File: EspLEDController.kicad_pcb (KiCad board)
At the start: 4 copper layers, 100 x 95 mm, 106 parts, among them J1 USB_B_Micro, J10 Conn_01x02, J11 Conn_01x02, J12 Conn_01x02, J13 Conn_01x02, J14 Conn_01x02, J15 Conn_01x02, J16 Conn_01x02, J17 Conn_01x02, J18 Conn_01x02, J19 Conn_01x02, J2 FTDI, J20 Conn_01x02, J21 Conn_01x02, J22 Conn_01x02, J23 Conn_01x02, J24 Conn_01x02, J25 Conn_01x02, J26 Conn_01x02, J27 Conn_01x02, J28 Conn_01x02, J29 Conn_01x02, J3 FLASH, J30 Conn_01x02, J31 Conn_01x02, J32 Conn_01x02, J33 Conn_01x02, J34 Conn_01x02, J35 Conn_01x02, J36 Conn_01x02, J37 Conn_01x02, J38 Conn_01x02, J39 Conn_01x02, J4 Conn_01x02, J40 Conn_01x02, J41 Conn_01x02, J42 Conn_01x02, J43 Conn_01x02, J44 Conn_01x02, J45 Conn_01x02, J5 Conn_01x02, J6 Conn_01x02, J7 Conn_01x02, J8 Conn_01x02, J9 Conn_01x02, SW1 RESET, SW2 FLASH, U1 ESP-12F, U10 WS2811, U11 WS2811, U12 WS2811, U13 WS2811, U14 WS2811, U15 WS2811, U16 WS2811, U17 74AHCT1G125, U2 AMS1117-3.3, U3 WS2811, U4 WS2811, U5 WS2811, U6 WS2811, U7 WS2811, U8 WS2811, U9 WS2811

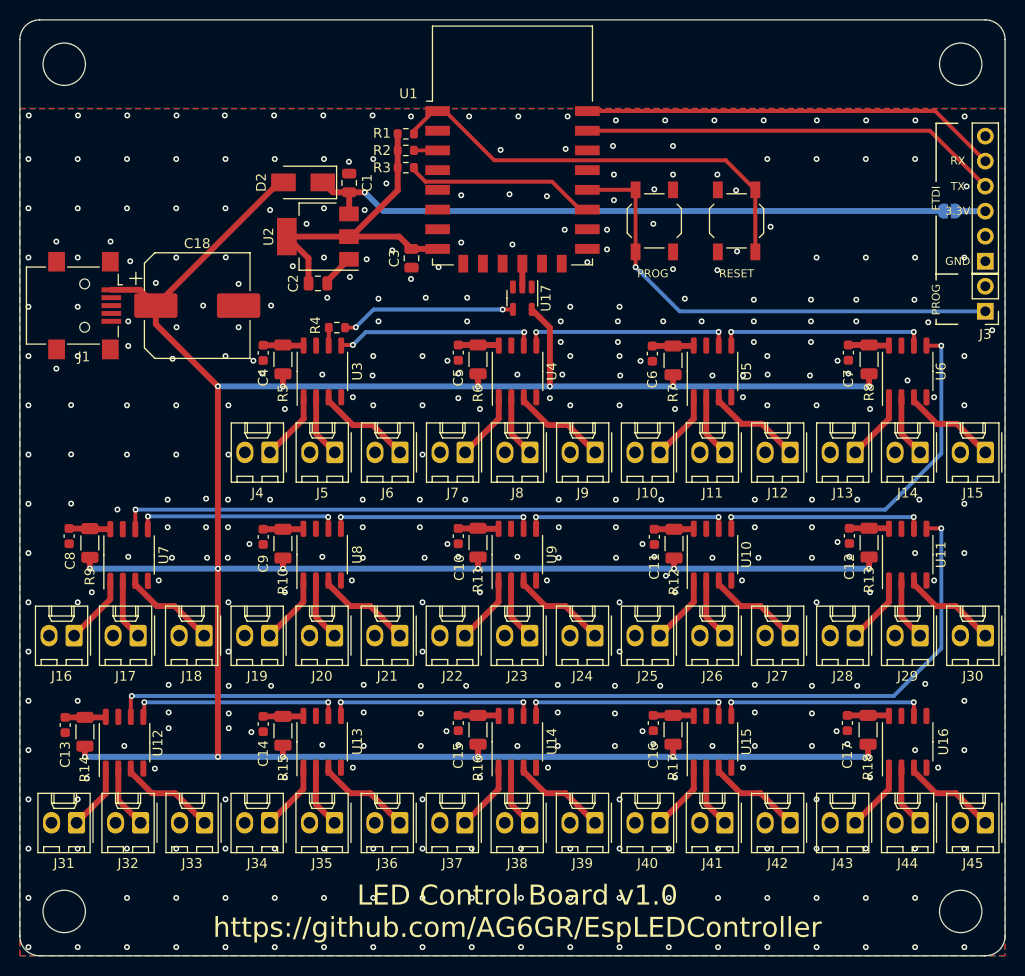
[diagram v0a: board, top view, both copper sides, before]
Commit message: v1.1 Fix LED headers, FTDI power
Fixes from first board rev:
	- Fix LEDs to be between power and driver output
	- Change FTDI header power to 5V
	- Remove now redundant diode on FTDI power input
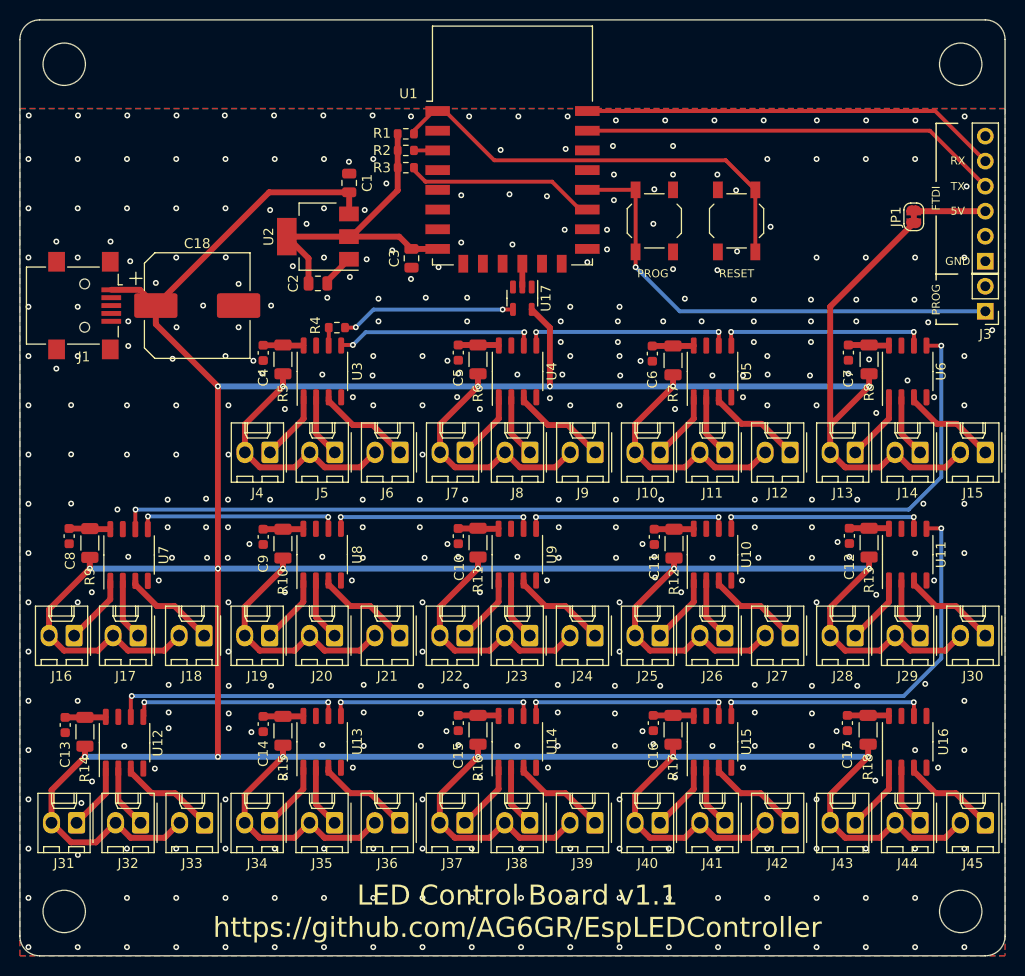
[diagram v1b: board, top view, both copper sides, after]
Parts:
- removed D2: D, Diode_SMD:D_SMA
- JP1: moved to F.Cu
- moved JP1 3.66 mm to (165.7, 47.0), turned to 90 degrees
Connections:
- C1 pad 1: +3.3VP -> +5V
- J10 pad 2: GND -> +5V
- J11 pad 2: GND -> +5V
- J12 pad 2: GND -> +5V
- J13 pad 2: GND -> +5V
- J14 pad 2: GND -> +5V
- J15 pad 2: GND -> +5V
- J16 pad 2: GND -> +5V
- J17 pad 2: GND -> +5V
- J18 pad 2: GND -> +5V
- J19 pad 2: GND -> +5V
- J20 pad 2: GND -> +5V
- J21 pad 2: GND -> +5V
- J22 pad 2: GND -> +5V
- J23 pad 2: GND -> +5V
- J24 pad 2: GND -> +5V
- J25 pad 2: GND -> +5V
- J26 pad 2: GND -> +5V
- J27 pad 2: GND -> +5V
- J28 pad 2: GND -> +5V
- J29 pad 2: GND -> +5V
- J30 pad 2: GND -> +5V
- J31 pad 2: GND -> +5V
- J32 pad 2: GND -> +5V
- J33 pad 2: GND -> +5V
- J34 pad 2: GND -> +5V
- J35 pad 2: GND -> +5V
- J36 pad 2: GND -> +5V
- J37 pad 2: GND -> +5V
- J38 pad 2: GND -> +5V
- J39 pad 2: GND -> +5V
- J4 pad 2: GND -> +5V
- J40 pad 2: GND -> +5V
- J41 pad 2: GND -> +5V
- J42 pad 2: GND -> +5V
- J43 pad 2: GND -> +5V
- J44 pad 2: GND -> +5V
- J45 pad 2: GND -> +5V
- J5 pad 2: GND -> +5V
- J6 pad 2: GND -> +5V
- J7 pad 2: GND -> +5V
- J8 pad 2: GND -> +5V
- J9 pad 2: GND -> +5V
- JP1 pad 1: +3.3VP -> +5V
- U2 pad 3: +3.3VP -> +5V
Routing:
- net +5V: track 321.7 -> 691.4 mm
- net +3.3VP: track 66.4 -> 0.00 mm, vias 1 -> 0
- net Net-(J2-Pad3): track 3.04 -> 7.30 mm
- net /WS2811Unit3/DO: track 98.6 -> 100.0 mm
- net /WS2811Unit8/DO: track 100.0 -> 100.6 mm
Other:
- board text added: "5V"
- board text added: "LED Control Board v1.1 https://github.com/AG6GR/EspLEDController"
- board text removed: "3.3V"
- board text removed: "LED Control Board v1.0 https://github.com/AG6GR/EspLEDController"

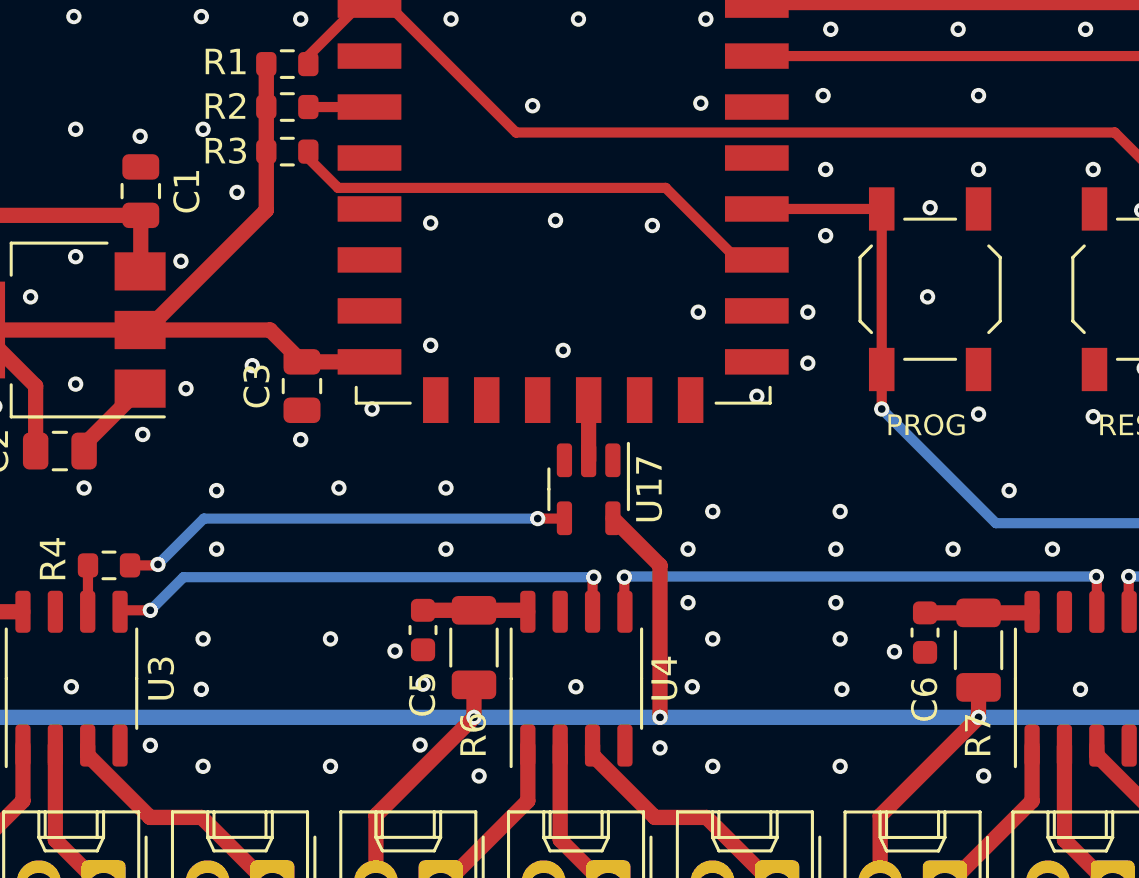
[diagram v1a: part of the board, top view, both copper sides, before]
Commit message: Fix incorrect ESP8266 GPIO pin
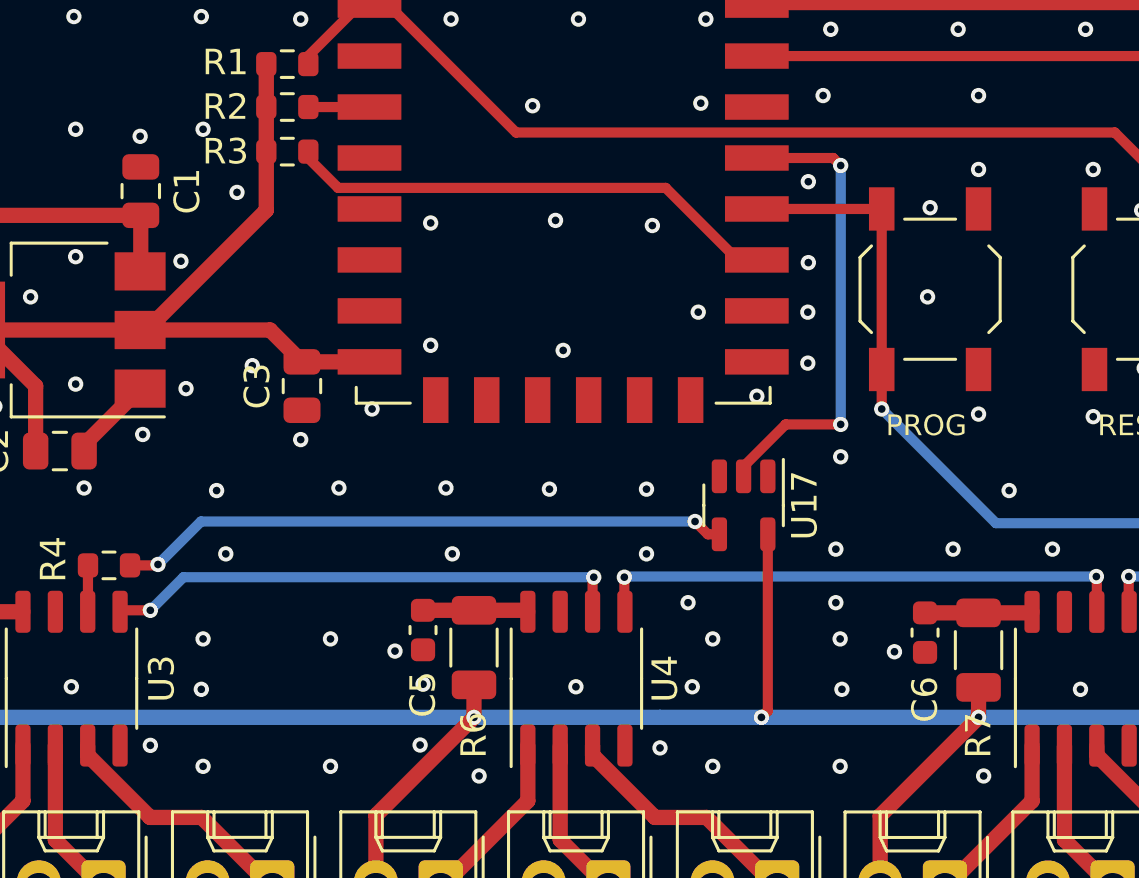
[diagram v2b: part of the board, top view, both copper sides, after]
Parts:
- moved U17 6.11 mm to (132.1, 55.9)
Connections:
- U1 pad 12: LED_GPIO -> unconnected-(U1-Pad12)
- U1 pad 19: unconnected-(U1-Pad19) -> LED_GPIO
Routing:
- net LED_GPIO: track 2.36 -> 18.5 mm, vias 0 -> 2
- net Net-(R4-Pad1): track 17.8 -> 24.0 mm
- net +5V: track 691.4 -> 690.1 mm
- net GND: vias 368 -> 369
